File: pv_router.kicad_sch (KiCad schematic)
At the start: 13 parts, among them IC1 ADS131M03IPWR, J1 AudioJack3, J2 AudioJack3, J4 Barrel_Jack_Switch_Pin3Ring, J5 USB_B_Mini, U1 ATmega328-P, U2 oscillator

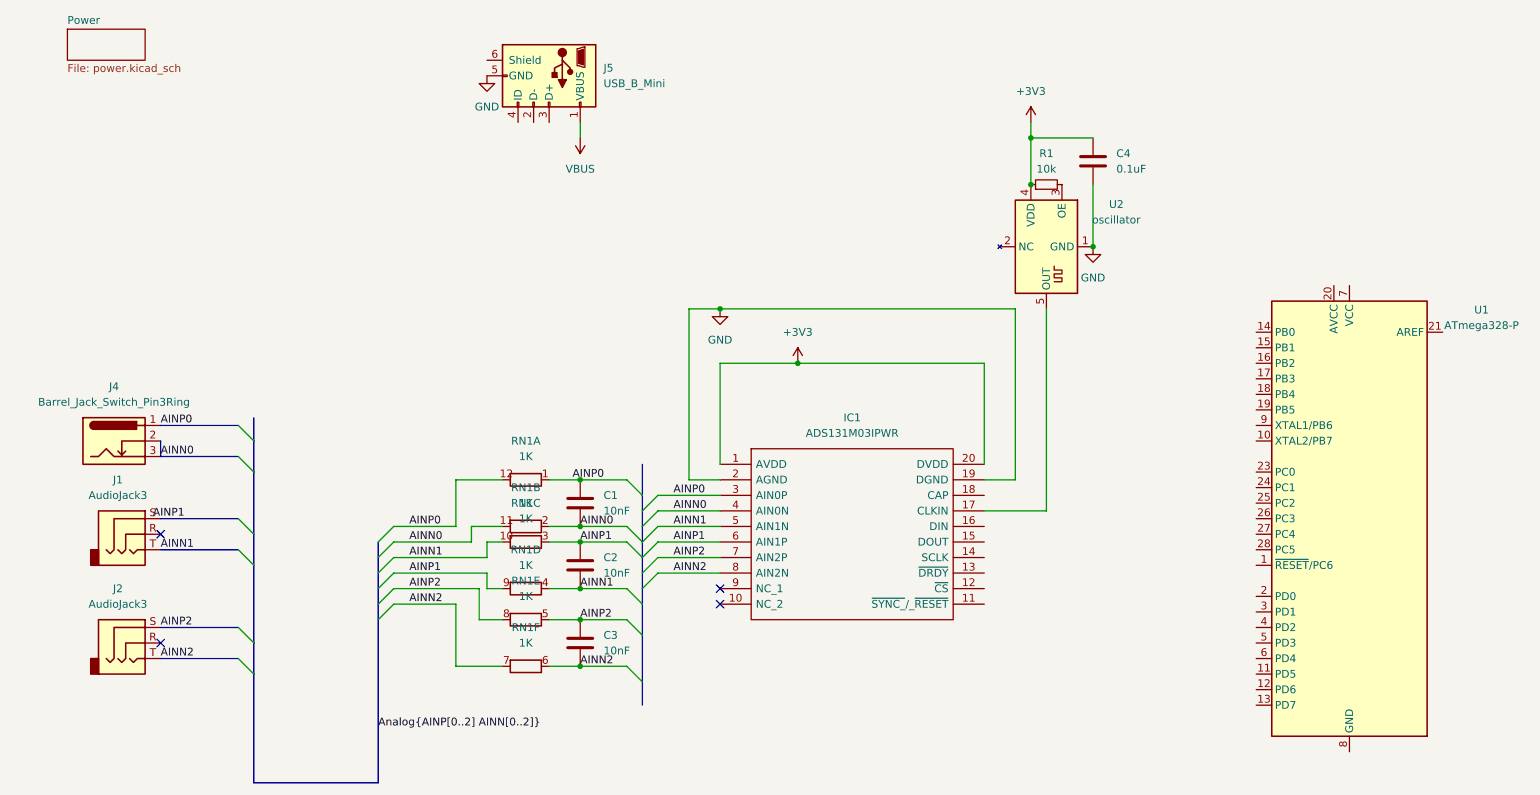
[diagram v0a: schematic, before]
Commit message: lib: add ATM M90E26 AFE
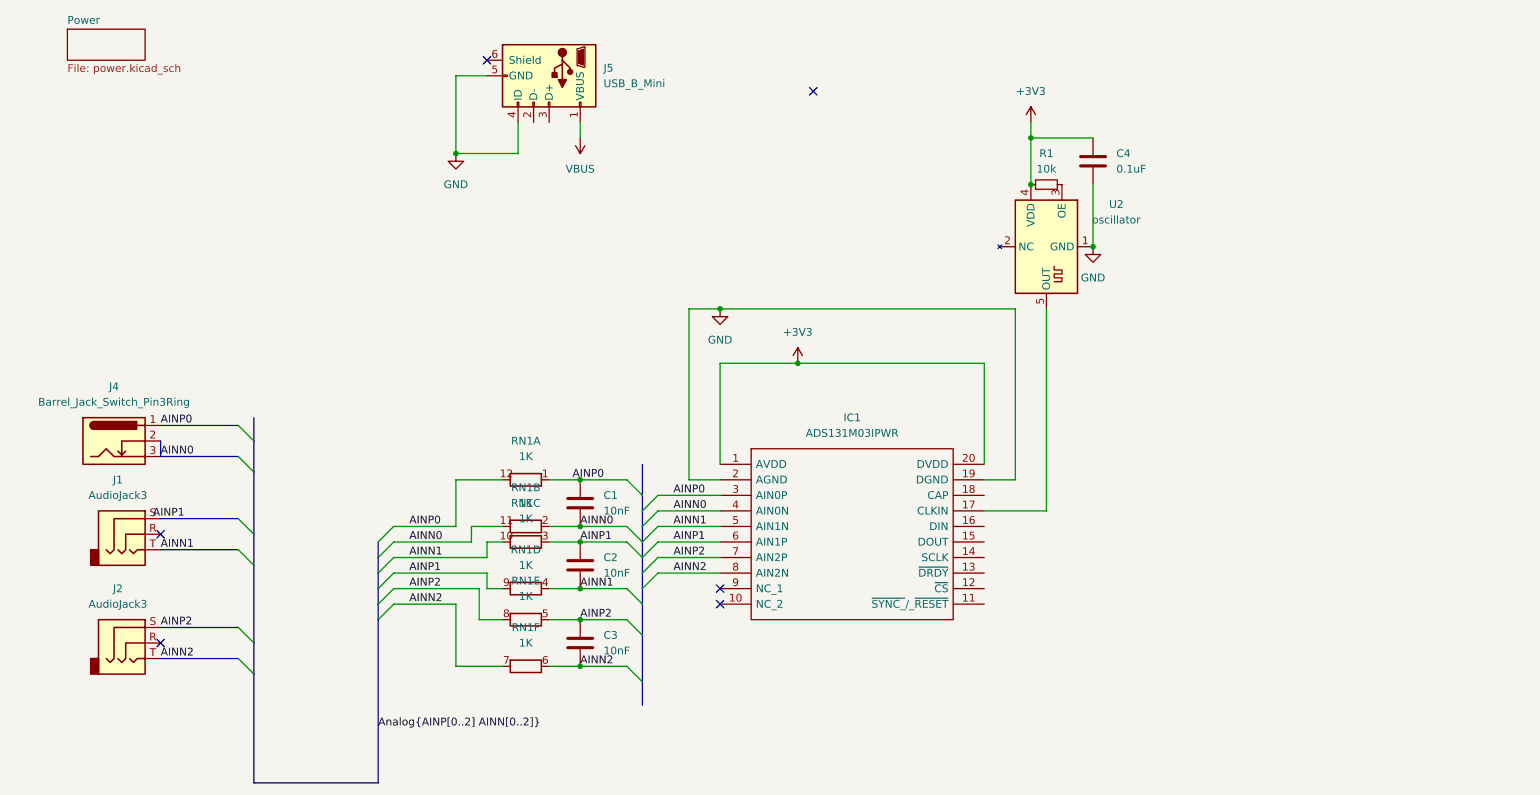
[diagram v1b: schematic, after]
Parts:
- removed U1: ATmega328-P, Package_DIP:DIP-28_W7.62mm, symbol MCU_Microchip_ATmega:ATmega328-P
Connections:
- net GND: now also J5.4 (ID)
- no-connect marks 4 -> 6
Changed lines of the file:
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@@
   (junction (at 172.72 35.56) (diameter 0) (color 0 0 0 0)
+  )
+  (junction (at 78.74 38.1) (diameter 0) (color 0 0 0 0)
   )
   (junction (at 99.06 101.6) (diameter 0) (color 0 0 0 0)
@@
   (no_connect (at 121.92 109.22))
   (no_connect (at 30.48 118.11))
+  (no_connect (at 83.82 22.86))
+  (no_connect (at 137.16 27.94))
   (no_connect (at 121.92 111.76))
   (bus_entry (at 43.18 120.65) (size 2.54 2.54)
@@
     (stroke (width 0) (type default))
   )
+  (wire (pts (xy 88.9 33.02) (xy 88.9 38.1))
+    (stroke (width 0) (type default))
+  )
+  (wire (pts (xy 83.82 25.4) (xy 78.74 25.4))
+    (stroke (width 0) (type default))
+  )
   (wire (pts (xy 83.82 104.14) (xy 83.82 101.6))
     (stroke (width 0) (type default))
@@
     (stroke (width 0) (type default))
   )
+  (wire (pts (xy 78.74 25.4) (xy 78.74 38.1))
+    (stroke (width 0) (type default))
+  )
   (wire (pts (xy 99.06 114.3) (xy 106.68 114.3))
     (stroke (width 0) (type default))
@@
   )
   (bus (pts (xy 66.04 109.22) (xy 66.04 111.76))
+    (stroke (width 0) (type default))
+  )
+  (wire (pts (xy 78.74 38.1) (xy 88.9 38.1))
     (stroke (width 0) (type default))
   )
@@
     )
   )
-  (symbol (lib_id "power:GND") (at 83.82 25.4 0) (unit 1)
-    (in_bom yes) (on_board yes) (dnp no) (fields_autoplaced)
-    (property "Reference" "#PWR011" (at 83.82 31.75 0)
-      (effects (font (size 1.27 1.27)) hide)
-    )
-    (property "Value" "GND" (at 83.82 30.48 0)
-      (effects (font (size 1.27 1.27)))
-    )
-    (property "Footprint" "" (at 83.82 25.4 0)
-      (effects (font (size 1.27 1.27)) hide)
-    )
-    (property "Datasheet" "" (at 83.82 25.4 0)
+  (symbol (lib_id "power:GND") (at 78.74 38.1 0) (unit 1)
+    (in_bom yes) (on_board yes) (dnp no) (fields_autoplaced)
+    (property "Reference" "#PWR011" (at 78.74 44.45 0)
+      (effects (font (size 1.27 1.27)) hide)
+    )
+    (property "Value" "GND" (at 78.74 43.18 0)
+      (effects (font (size 1.27 1.27)))
+    )
+    (property "Footprint" "" (at 78.74 38.1 0)
+      (effects (font (size 1.27 1.27)) hide)
+    )
+    (property "Datasheet" "" (at 78.74 38.1 0)
       (effects (font (size 1.27 1.27)) hide)
     )
@@
         )
       )
-    )
-  )
-  (symbol (lib_id "MCU_Microchip_ATmega:ATmega328-P") (at 224.79 97.79 0) (mirror y) (unit 1)
-    (in_bom yes) (on_board yes) (dnp no)
-    (property "Reference" "U1" (at 246.38 63.6621 0)
-      (effects (font (size 1.27 1.27)))
-    )
-    (property "Value" "ATmega328-P" (at 246.38 66.2021 0)
-      (effects (font (size 1.27 1.27)))
-    )
-    (property "Footprint" "Package_DIP:DIP-28_W7.62mm" (at 224.79 97.79 0)
-      (effects (font (size 1.27 1.27) italic) hide)
-    )
-    (property "Datasheet" "http://ww1.microchip.com/downloads/en/DeviceDoc/ATmega328_P%20AVR%20MCU%20with%20picoPower%20Technology%20Data%20Sheet%2040001984A.pdf" (at 224.79 97.79 0)
-      (effects (font (size 1.27 1.27)) hide)
-    )
-    (pin "27")
-    (pin "15")
-    (pin "2")
-    (pin "25")
-    (pin "7")
-    (pin "8")
-    (pin "9")
-    (pin "21")
-    (pin "10")
-    (pin "26")
-    (pin "20")
-    (pin "12")
-    (pin "18")
-    (pin "28")
-    (pin "23")
-    (pin "24")
-    (pin "16")
-    (pin "4")
-    (pin "13")
-    (pin "22")
-    (pin "11")
-    (pin "6")
-    (pin "19")
-    (pin "17")
-    (pin "3")
-    (pin "5")
-    (pin "14")
-    (pin "1")
-    (instances
-      (project "pv_router"
-        (path "/08ef31dc-81c2-4bcd-8336-e62c344e451e"
-          (reference "U1") (unit 1)
-        )
-      )

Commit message: feat: add adc component and associated sheet
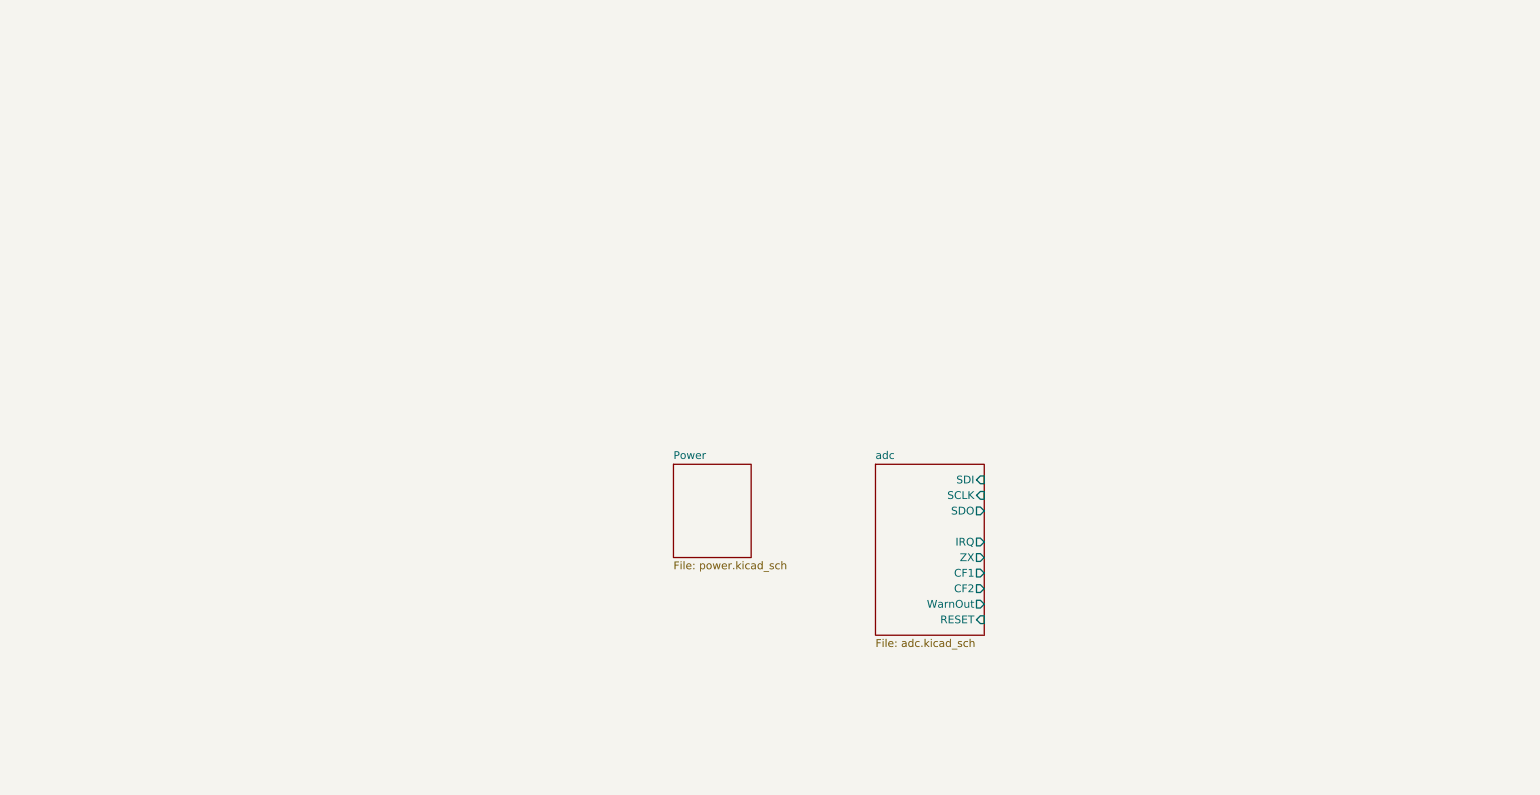
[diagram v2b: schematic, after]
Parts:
- removed C1, C2, C3: 10nF, symbol Device:C
- removed C4: 0.1uF, symbol Device:C
- removed IC1: ADS131M03IPWR, SOP65P640X120-20N, symbol ADS131M03IPWR:ADS131M03IPWR
- removed J1: AudioJack3, Connector_Audio:Jack_3.5mm_CUI_SJ1-3523N_Horizontal, symbol Connector_Audio:AudioJack3
- removed J2: AudioJack3, symbol Connector_Audio:AudioJack3
- removed J4: Barrel_Jack_Switch_Pin3Ring, symbol Connector:Barrel_Jack_Switch_Pin3Ring
- removed J5: USB_B_Mini, symbol Connector:USB_B_Mini
- removed R1: 10k, symbol Device:R_Small
- removed RN1: 1K, symbol Device:R_Pack06_Split
- removed U2: oscillator, Package_TO_SOT_SMD:SOT-23-5_HandSoldering, symbol PVrouter:oscillator
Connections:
- no-connect marks 6 -> 0
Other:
- added sheet adc (adc.kicad_sch)

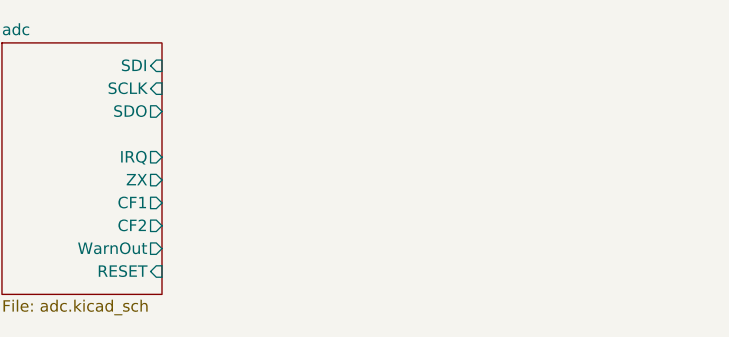
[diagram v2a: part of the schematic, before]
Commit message: feat: add esp32 component
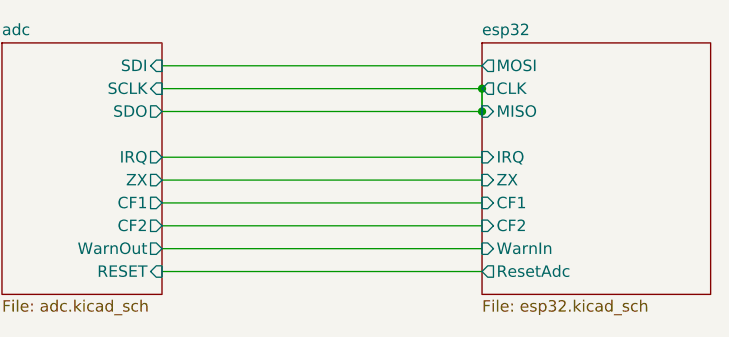
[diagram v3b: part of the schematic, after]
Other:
- added sheet esp32 (esp32.kicad_sch)
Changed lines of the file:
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@@
 (kicad_sch (version 20230121) (generator eeschema)
   (paper "A4")
+  (junction (at 200.66 93.98) (diameter 0) (color 0 0 0 0)
+  )
+  (junction (at 200.66 96.52) (diameter 0) (color 0 0 0 0)
+  )
+  (wire (pts (xy 165.1 104.14) (xy 200.66 104.14))
+    (stroke (width 0) (type default))
+  )
+  (wire (pts (xy 165.1 101.6) (xy 200.66 101.6))
+    (stroke (width 0) (type default))
+  )
+  (wire (pts (xy 165.1 109.22) (xy 200.66 109.22))
+    (stroke (width 0) (type default))
+  )
+  (wire (pts (xy 165.1 114.3) (xy 200.66 114.3))
+    (stroke (width 0) (type default))
+  )
+  (wire (pts (xy 165.1 96.52) (xy 200.66 96.52))
+    (stroke (width 0) (type default))
+  )
+  (wire (pts (xy 200.66 96.52) (xy 200.66 93.98))
+    (stroke (width 0) (type default))
+  )
+  (wire (pts (xy 165.1 106.68) (xy 200.66 106.68))
+    (stroke (width 0) (type default))
+  )
+  (wire (pts (xy 165.1 111.76) (xy 200.66 111.76))
+    (stroke (width 0) (type default))
+  )
+  (wire (pts (xy 165.1 91.44) (xy 200.66 91.44))
+    (stroke (width 0) (type default))
+  )
+  (wire (pts (xy 165.1 93.98) (xy 200.66 93.98))
+    (stroke (width 0) (type default))
+  )
+  (sheet (at 200.66 88.9) (size 25.4 27.94) (fields_autoplaced)
+    (stroke (width 0.1524) (type solid))
+    (fill (color 0 0 0 0.0000))
+    (property "Sheetname" "esp32" (at 200.66 88.1884 0)
+      (effects (font (size 1.27 1.27)) (justify left bottom))
+    )
+    (property "Sheetfile" "esp32.kicad_sch" (at 200.66 117.4246 0)
+      (effects (font (size 1.27 1.27)) (justify left top))
+    )
+    (pin "CF1" input (at 200.66 106.68 180)
+      (effects (font (size 1.27 1.27)) (justify left))
+    )
+    (pin "CF2" input (at 200.66 109.22 180)
+      (effects (font (size 1.27 1.27)) (justify left))
+    )
+    (pin "MOSI" output (at 200.66 91.44 180)
+      (effects (font (size 1.27 1.27)) (justify left))
+    )
+    (pin "CLK" output (at 200.66 93.98 180)
+      (effects (font (size 1.27 1.27)) (justify left))
+    )
+    (pin "MISO" input (at 200.66 96.52 180)
+      (effects (font (size 1.27 1.27)) (justify left))
+    )
+    (pin "ResetAdc" output (at 200.66 114.3 180)
+      (effects (font (size 1.27 1.27)) (justify left))
+    )
+    (pin "IRQ" input (at 200.66 101.6 180)
+      (effects (font (size 1.27 1.27)) (justify left))
+    )
+    (pin "WarnIn" input (at 200.66 111.76 180)
+      (effects (font (size 1.27 1.27)) (justify left))
+    )
+    (pin "ZX" input (at 200.66 104.14 180)
+      (effects (font (size 1.27 1.27)) (justify left))
+    )
+    (instances
+      (project "pv_router"
+        (path "/08ef31dc-81c2-4bcd-8336-e62c344e451e" (page "4"))
+      )
+    )
+  )
   (sheet (at 114.3 88.9) (size 12.7 15.24) (fields_autoplaced)
     (stroke (width 0.1524) (type solid))
